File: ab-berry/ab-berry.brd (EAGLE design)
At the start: 58.4 x 61 mm, 39 parts, among them U1 LM1117MPX-3.3/NOPB or AP2114H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

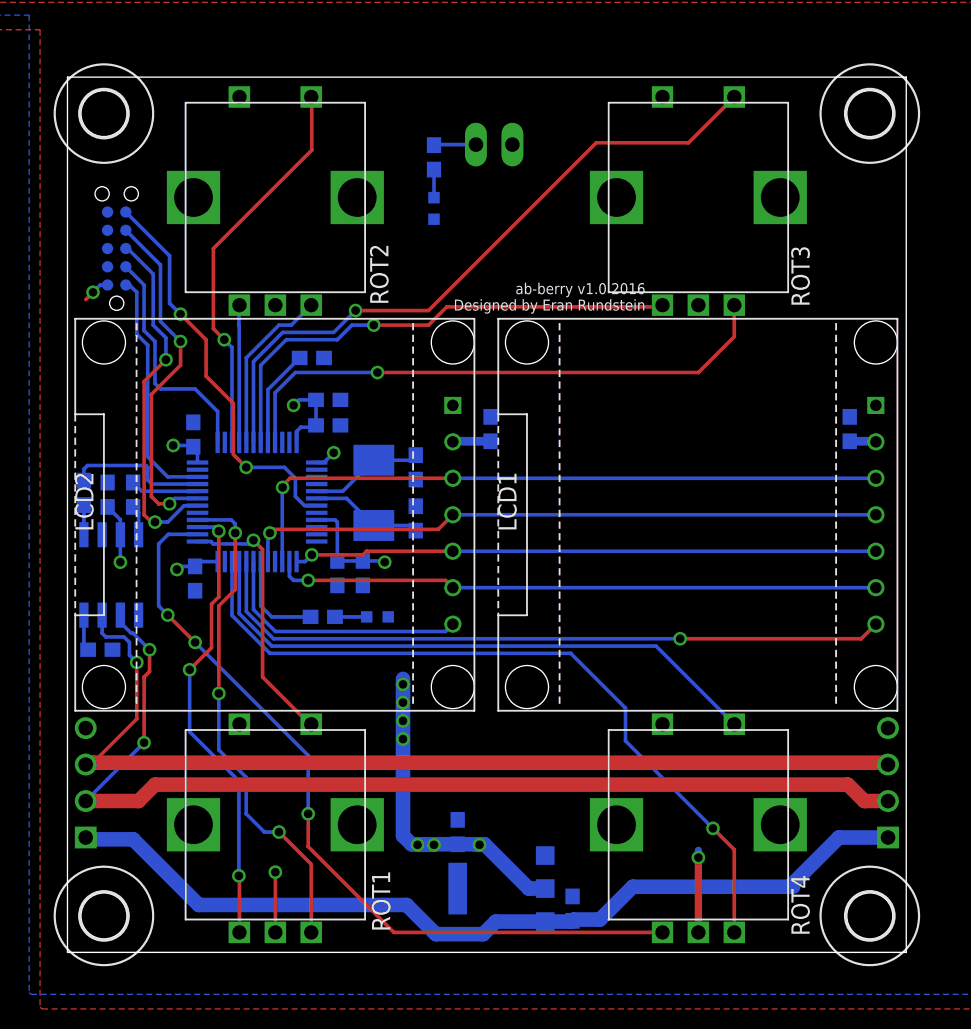
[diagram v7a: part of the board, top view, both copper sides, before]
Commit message: add pushbutton
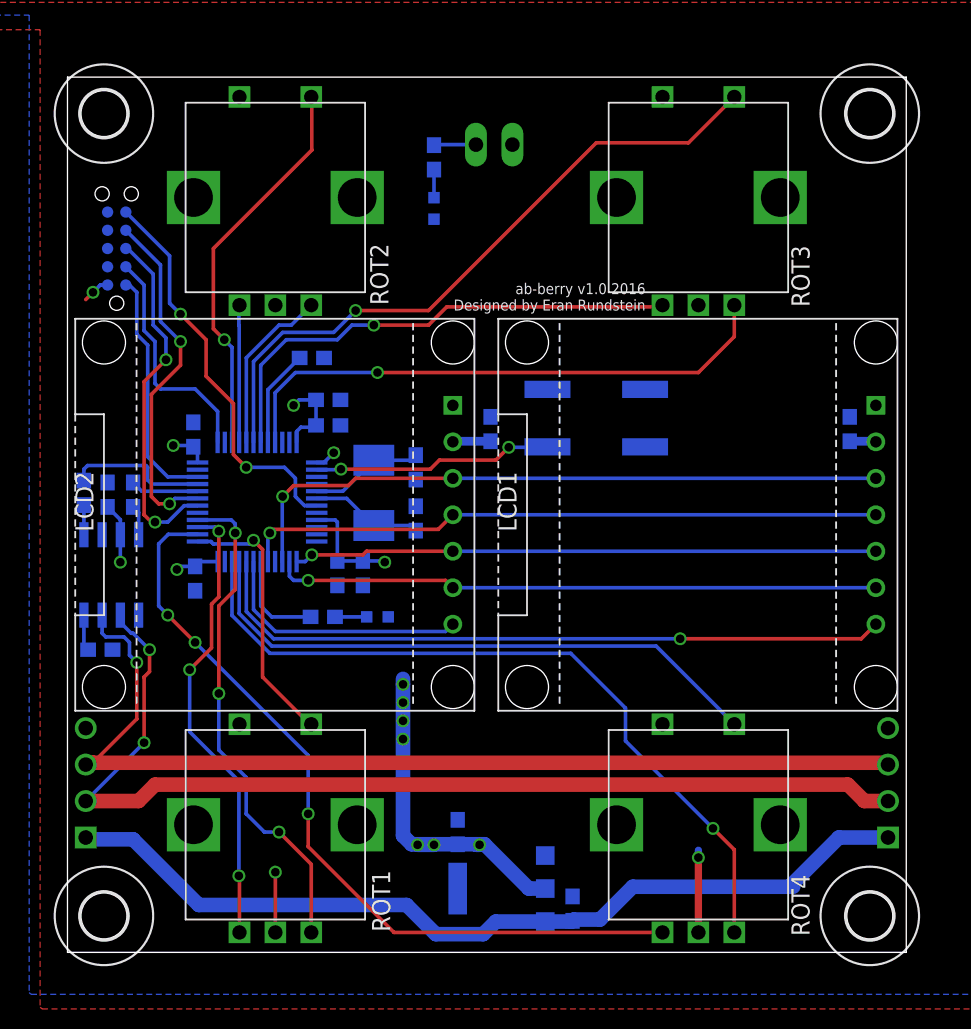
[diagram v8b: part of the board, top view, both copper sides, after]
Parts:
- added USR: (no value), microbuilder:EVQ-Q2
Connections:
- new net BTN_USR: STM32F072CBT6.2, USR.B
- net GND: now also USR.A
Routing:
- net BTN_USR: track 0.00 -> 16.7 mm, vias 0 -> 2
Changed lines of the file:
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@@
 <setting verticaltext="up"/>
 </settings>
-<grid distance="5" unitdist="mil" unit="mil" style="lines" multiple="1" display="no" altdistance="0.025" altunitdist="inch" altunit="inch"/>
+<grid distance="5" unitdist="mil" unit="mm" style="lines" multiple="1" display="no" altdistance="0.025" altunitdist="inch" altunit="inch"/>
 <layers>
 <layer number="1" name="Top" color="4" fill="1" visible="yes" active="yes"/>
@@
 </class>
 </classes>
-<designrules name="oshpark *">
+<designrules name="Fusion_eagle_rule_v1.1">
 <description language="de">&lt;b&gt;EAGLE Design Rules&lt;/b&gt;
 &lt;p&gt;
@@
 Einstellungen hier und speichern die Design Rules unter
 einem neuen Namen ab.</description>
-<description language="en">&lt;b&gt;Laen's PCB Order Design Rules&lt;/b&gt;
+<description language="en">&lt;b&gt;EAGLE Design Rules&lt;/b&gt;
 &lt;p&gt;
-Please make sure your boards conform to these design rules.</description>
+The default Design Rules have been set to cover
+a wide range of applications. Your particular design
+may have different requirements, so please make the
+necessary adjustments and save your customized
+design rules under a new name.</description>
+<description language="zh">&lt;b&gt;Seeed Studio EAGLE Design Rules&lt;/b&gt;
+</description>
 <param name="layerSetup" value="(1*16)"/>
-<param name="mtCopper" value="0.0356mm 0.0356mm 0.0356mm 0.0356mm 0.0356mm 0.0356mm 0.0356mm 0.0356mm 0.0356mm 0.0356mm 0.0356mm 0.0356mm 0.0356mm 0.0356mm 0.0356mm 0.0356mm"/>
-<param name="mtIsolate" value="1.5011mm 0.1499mm 0.2007mm 0.1499mm 0.2007mm 0.1499mm 0.2007mm 0.1499mm 0.2007mm 0.1499mm 0.2007mm 0.1499mm 0.2007mm 0.1499mm 0.2007mm"/>
+<param name="mtCopper" value="0.035mm 0.035mm 0.035mm 0.035mm 0.035mm 0.035mm 0.035mm 0.035mm 0.035mm 0.035mm 0.035mm 0.035mm 0.035mm 0.035mm 0.035mm 0.035mm"/>
+<param name="mtIsolate" value="1.5mm 0.15mm 0.2mm 0.15mm 0.2mm 0.15mm 0.2mm 0.15mm 0.2mm 0.15mm 0.2mm 0.15mm 0.2mm 0.15mm 0.2mm"/>
 <param name="mdWireWire" value="6mil"/>
 <param name="mdWirePad" value="6mil"/>
@@
 <param name="mdPadVia" value="6mil"/>
 <param name="mdViaVia" value="6mil"/>
-<param name="mdSmdPad" value="6mil"/>
-<param name="mdSmdVia" value="6mil"/>
-<param name="mdSmdSmd" value="6mil"/>
+<param name="mdSmdPad" value="0mil"/>
+<param name="mdSmdVia" value="0mil"/>
+<param name="mdSmdSmd" value="0mil"/>
 <param name="mdViaViaSameLayer" value="8mil"/>
 <param name="mnLayersViaInSmd" value="2"/>
-<param name="mdCopperDimension" value="15mil"/>
-<param name="mdDrill" value="6mil"/>
+<param name="mdCopperDimension" value="10mil"/>
+<param name="mdDrill" value="10mil"/>
 <param name="mdSmdStop" value="0mil"/>
 <param name="msWidth" value="6mil"/>
-<param name="msDrill" value="13mil"/>
-<param name="msMicroVia" value="13mil"/>
+<param name="msDrill" value="12mil"/>
+<param name="msMicroVia" value="12mil"/>
 <param name="msBlindViaRatio" value="0.5"/>
 <param name="rvPadTop" value="0.25"/>
@@
 <param name="rvMicroViaOuter" value="0.25"/>
 <param name="rvMicroViaInner" value="0.25"/>
-<param name="rlMinPadTop" value="7mil"/>
+<param name="rlMinPadTop" value="10mil"/>
 <param name="rlMaxPadTop" value="20mil"/>
-<param name="rlMinPadInner" value="7mil"/>
+<param name="rlMinPadInner" value="10mil"/>
 <param name="rlMaxPadInner" value="20mil"/>
-<param name="rlMinPadBottom" value="7mil"/>
+<param name="rlMinPadBottom" value="10mil"/>
 <param name="rlMaxPadBottom" value="20mil"/>
-<param name="rlMinViaOuter" value="7mil"/>
+<param name="rlMinViaOuter" value="6mil"/>
 <param name="rlMaxViaOuter" value="20mil"/>
-<param name="rlMinViaInner" value="7mil"/>
+<param name="rlMinViaInner" value="6mil"/>
 <param name="rlMaxViaInner" value="20mil"/>
 <param name="rlMinMicroViaOuter" value="4mil"/>
@@
 <param name="psTop" value="-1"/>
 <param name="psBottom" value="-1"/>
-<param name="psFirst" value="-1"/>
+<param name="psFirst" value="0"/>
 <param name="psElongationLong" value="100"/>
 <param name="psElongationOffset" value="100"/>
 <param name="mvStopFrame" value="1"/>
 <param name="mvCreamFrame" value="0"/>
-<param name="mlMinStopFrame" value="3mil"/>
-<param name="mlMaxStopFrame" value="3mil"/>
+<param name="mlMinStopFrame" value="2mil"/>
+<param name="mlMaxStopFrame" value="2mil"/>
 <param name="mlMinCreamFrame" value="0mil"/>
 <param name="mlMaxCreamFrame" value="0mil"/>
-<param name="mlViaStopLimit" value="0mil"/>
+<param name="mlViaStopLimit" value="100mil"/>
 <param name="srRoundness" value="0"/>
 <param name="srMinRoundness" value="0mil"/>
@@
 <param name="dpGapFactor" value="2.5"/>
 <param name="checkGrid" value="0"/>
-<param name="checkAngle" value="1"/>
+<param name="checkAngle" value="0"/>
 <param name="checkFont" value="1"/>
-<param name="checkRestrict" value="1"/>
+<param name="checkRestrict" value="0"/>
 <param name="useDiameter" value="13"/>
 <param name="maxErrors" value="50"/>
@@
 </element>
 <element name="U$36" library="keves" package="ABM7-8.000MHZ-D2Y-T" value="ABM7-8.000MHZ-D2Y-T" x="21.336" y="32.004" rot="MR90"/>
+<element name="USR" library="microbuilder" package="EVQ-Q2" value="" x="36.83" y="37.211" rot="MR180"/>
 </elements>
 <signals>
@@
 <contactref element="C13" pad="2"/>
 <contactref element="C12" pad="1"/>
+<contactref element="USR" pad="A"/>
 </signal>
 <signal name="3.3V">
@@
 <contactref element="STM32F072CBT6" pad="15"/>
 <wire x1="56.304" y1="33.02" x2="26.84" y2="33.02" width="0.254" layer="16"/>
-<via x="14.986" y="32.385" extent="1-16" drill="0.6"/>
-<wire x1="15.494" y1="33.02" x2="26.84" y2="33.02" width="0.254" layer="1"/>
-<wire x1="14.958" y1="27.219" x2="14.958" y2="32.357" width="0.254" layer="16"/>
-<wire x1="14.958" y1="32.357" x2="14.986" y2="32.385" width="0.254" layer="16"/>
-<wire x1="14.986" y1="32.385" x2="14.986" y2="32.512" width="0.254" layer="1"/>
-<wire x1="14.986" y1="32.512" x2="15.494" y2="33.02" width="0.254" layer="1"/>
+<via x="14.986" y="31.75" extent="1-16" drill="0.6"/>
+<wire x1="14.958" y1="27.219" x2="14.958" y2="31.722" width="0.254" layer="16"/>
+<wire x1="26.84" y1="33.02" x2="20.066" y2="33.02" width="0.254" layer="1"/>
+<wire x1="20.066" y1="33.02" x2="19.558" y2="32.512" width="0.254" layer="1"/>
+<wire x1="19.558" y1="32.512" x2="15.748" y2="32.512" width="0.254" layer="1"/>
+<wire x1="15.748" y1="32.512" x2="14.986" y2="31.75" width="0.254" layer="1"/>
+<wire x1="14.958" y1="31.722" x2="14.986" y2="31.75" width="0.254" layer="16"/>
 </signal>
 <signal name="LCD_CS2">
@@
 <wire x1="23.9023" y1="29.7307" x2="24.257" y2="29.376" width="0.254" layer="16"/>
 </signal>
+<signal name="BTN_USR">
+<contactref element="USR" pad="B"/>
+<contactref element="STM32F072CBT6" pad="2"/>
+<wire x1="17.358" y1="33.619" x2="19.014" y2="33.619" width="0.254" layer="16"/>
+<wire x1="19.014" y1="33.619" x2="19.05" y2="33.655" width="0.254" layer="16"/>
+<via x="19.05" y="33.655" extent="1-16" drill="0.6"/>
+<via x="30.734" y="35.179" extent="1-16" drill="0.6"/>
+<wire x1="29.845" y1="34.29" x2="30.734" y2="35.179" width="0.254" layer="1"/>
+<wire x1="30.734" y1="35.179" x2="33.398" y2="35.179" width="0.254" layer="16"/>
+<wire x1="33.398" y1="35.179" x2="33.43" y2="35.211" width="0.254" layer="16"/>
+<wire x1="19.05" y1="33.655" x2="25.273" y2="33.655" width="0.254" layer="1"/>
+<wire x1="25.273" y1="33.655" x2="25.908" y2="34.29" width="0.254" layer="1"/>
+<wire x1="25.908" y1="34.29" x2="29.845" y2="34.29" width="0.254" layer="1"/>
+</signal>
 </signals>
